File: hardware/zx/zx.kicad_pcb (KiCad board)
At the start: 2 copper layers, 71.6 x 59.9 mm, 46 parts, among them U1 CH559L, U2 CH446Q, Y1 12MHz

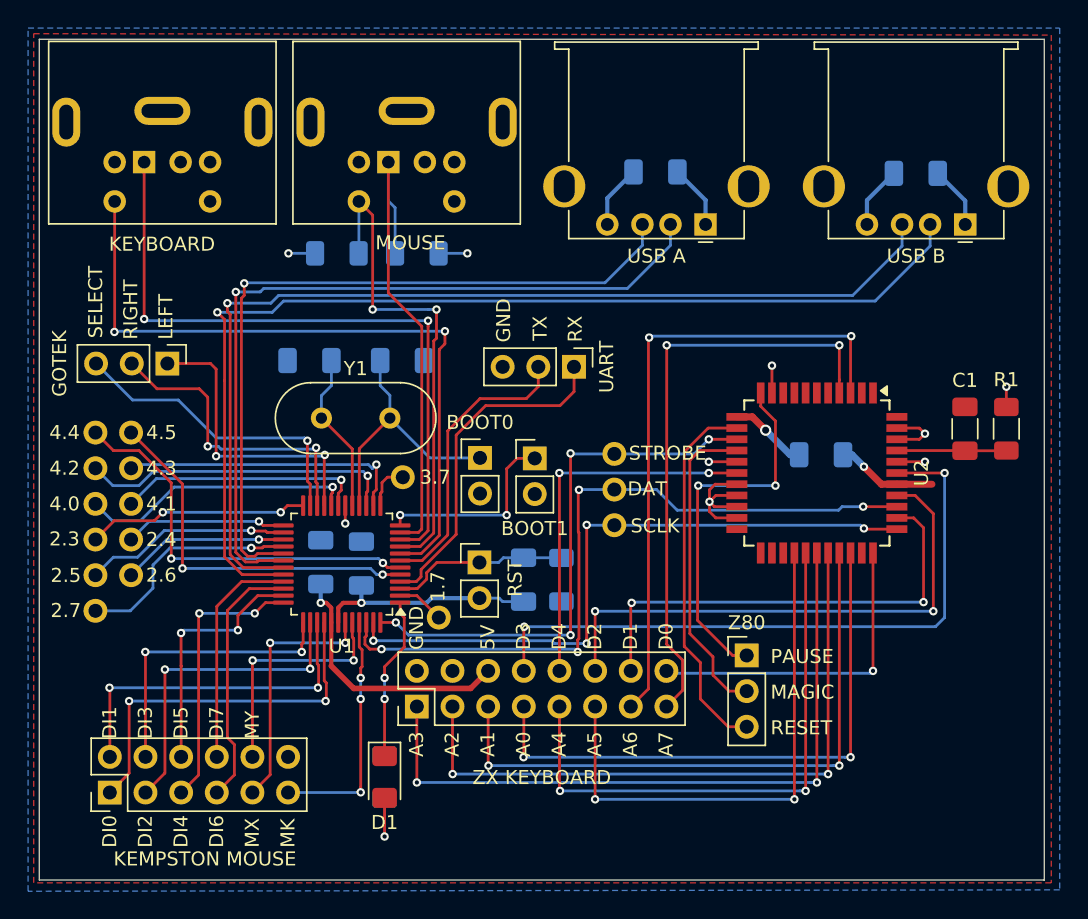
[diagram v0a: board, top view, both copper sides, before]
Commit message: PCB: replace +5V front face fill with tracks.
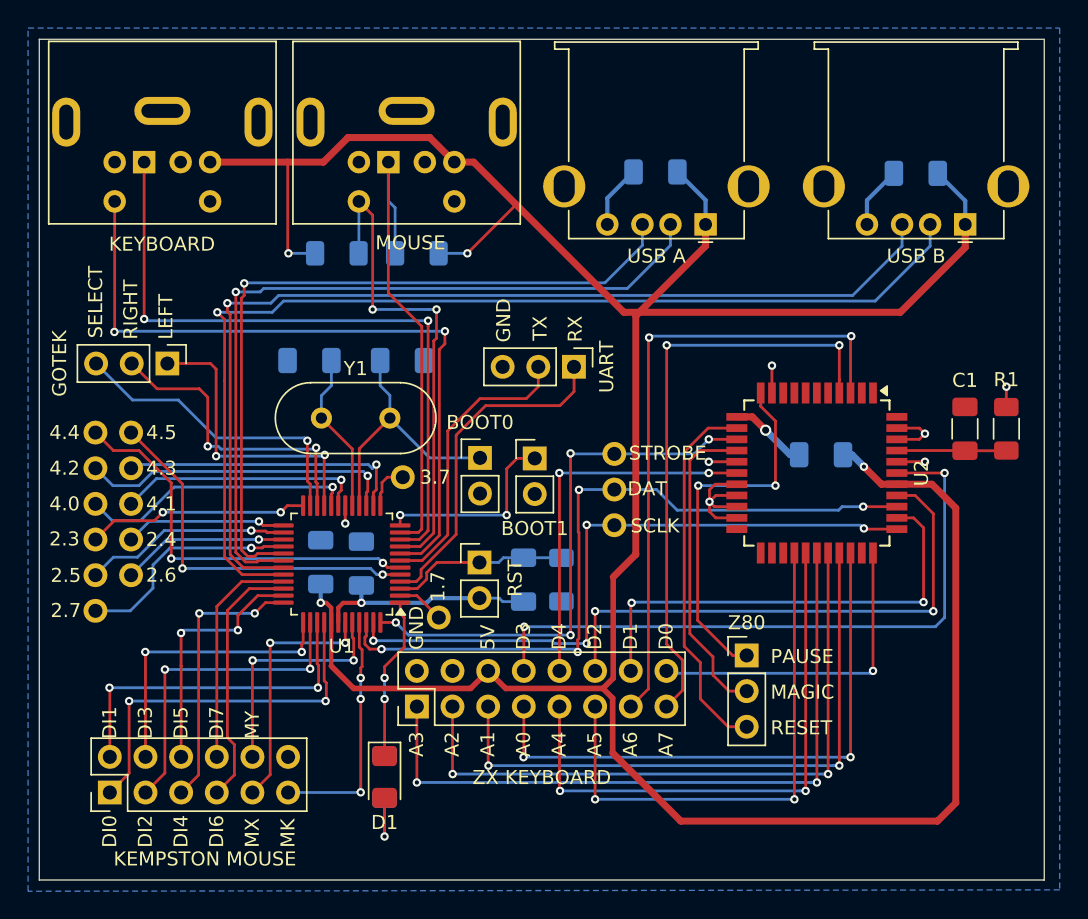
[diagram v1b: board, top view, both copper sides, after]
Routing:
- net +5V: track 38.9 -> 213.7 mm
- removed copper zone on F.Cu, net +5V
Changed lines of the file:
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@@
 	)
 	(segment
+		(start 130.95 108.75)
+		(end 129.57 108.75)
+		(width 0.5)
+		(layer "F.Cu")
+		(net 2)
+	)
+	(segment
+		(start 120.25 108.75)
+		(end 117.7 108.75)
+		(width 0.5)
+		(layer "F.Cu")
+		(net 2)
+	)
+	(segment
+		(start 140.85 150.85)
+		(end 145.7 155.7)
+		(width 0.5)
+		(layer "F.Cu")
+		(net 2)
+	)
+	(segment
 		(start 120.45 140.15)
 		(end 120.05 140.15)
@@
 	)
 	(segment
+		(start 164 155.7)
+		(end 165.3 154.4)
+		(width 0.5)
+		(layer "F.Cu")
+		(net 2)
+	)
+	(segment
+		(start 122 107)
+		(end 120.25 108.75)
+		(width 0.5)
+		(layer "F.Cu")
+		(net 2)
+	)
+	(segment
 		(start 122.4 146.25)
 		(end 120.8 144.65)
@@
 	)
 	(segment
+		(start 133.23 146.25)
+		(end 140.157767 146.25)
+		(width 0.4)
+		(layer "F.Cu")
+		(net 2)
+	)
+	(segment
+		(start 140.157767 146.25)
+		(end 140.89 145.517767)
+		(width 0.4)
+		(layer "F.Cu")
+		(net 2)
+	)
+	(segment
+		(start 140.89 145.517767)
+		(end 140.89 138.31)
+		(width 0.4)
+		(layer "F.Cu")
+		(net 2)
+	)
+	(segment
+		(start 140.157767 146.25)
+		(end 140.85 146.942233)
+		(width 0.4)
+		(layer "F.Cu")
+		(net 2)
+	)
+	(segment
+		(start 140.85 146.942233)
+		(end 140.85 150.85)
+		(width 0.4)
+		(layer "F.Cu")
+		(net 2)
+	)
+	(segment
+		(start 142.5 136.7)
+		(end 142.5 119.7)
+		(width 0.5)
+		(layer "F.Cu")
+		(net 2)
+	)
+	(segment
+		(start 161.35 119.45)
+		(end 165.97 114.83)
+		(width 0.5)
+		(layer "F.Cu")
+		(net 2)
+	)
+	(segment
+		(start 165.97 114.83)
+		(end 165.97 113.19)
+		(width 0.5)
+		(layer "F.Cu")
+		(net 2)
+	)
+	(segment
+		(start 142.75 119.45)
+		(end 161.35 119.45)
+		(width 0.5)
+		(layer "F.Cu")
+		(net 2)
+	)
+	(segment
 		(start 131.98 145)
 		(end 130.73 146.25)
@@
 	)
 	(segment
+		(start 117.7 115.2)
+		(end 117.7 108.75)
+		(width 0.2)
+		(layer "F.Cu")
+		(net 2)
+	)
+	(segment
+		(start 130.5 115.25)
+		(end 133.95 111.8)
+		(width 0.2)
+		(layer "F.Cu")
+		(net 2)
+	)
+	(segment
+		(start 145.7 155.7)
+		(end 164 155.7)
+		(width 0.5)
+		(layer "F.Cu")
+		(net 2)
+	)
+	(segment
+		(start 141.65 119.45)
+		(end 133.95 111.75)
+		(width 0.5)
+		(layer "F.Cu")
+		(net 2)
+	)
+	(segment
+		(start 140.89 138.31)
+		(end 142.5 136.7)
+		(width 0.5)
+		(layer "F.Cu")
+		(net 2)
+	)
+	(segment
+		(start 142.75 119.45)
+		(end 147.47 114.73)
+		(width 0.5)
+		(layer "F.Cu")
+		(net 2)
+	)
+	(segment
+		(start 142.75 119.45)
+		(end 141.65 119.45)
+		(width 0.5)
+		(layer "F.Cu")
+		(net 2)
+	)
+	(segment
+		(start 131.98 145)
+		(end 133.23 146.25)
+		(width 0.4)
+		(layer "F.Cu")
+		(net 2)
+	)
+	(segment
+		(start 165.3 133.4)
+		(end 163.6 131.7)
+		(width 0.5)
+		(layer "F.Cu")
+		(net 2)
+	)
+	(segment
+		(start 142.5 119.7)
+		(end 142.75 119.45)
+		(width 0.5)
+		(layer "F.Cu")
+		(net 2)
+	)
+	(segment
 		(start 130.73 146.25)
 		(end 122.4 146.25)
@@
 	)
 	(segment
+		(start 127.82 107)
+		(end 122 107)
+		(width 0.5)
+		(layer "F.Cu")
+		(net 2)
+	)
+	(segment
+		(start 117.7 108.75)
+		(end 112.17 108.75)
+		(width 0.5)
+		(layer "F.Cu")
+		(net 2)
+	)
+	(segment
 		(start 160 131.7)
 		(end 161.1 131.7)
@@
 	)
 	(segment
+		(start 133.95 111.8)
+		(end 133.95 111.75)
+		(width 0.2)
+		(layer "F.Cu")
+		(net 2)
+	)
+	(segment
 		(start 120.8 144.65)
 		(end 120.8 141.55)
@@
 	)
 	(segment
+		(start 165.3 154.4)
+		(end 165.3 133.4)
+		(width 0.5)
+		(layer "F.Cu")
+		(net 2)
+	)
+	(segment
+		(start 129.57 108.75)
+		(end 127.82 107)
+		(width 0.5)
+		(layer "F.Cu")
+		(net 2)
+	)
+	(segment
+		(start 133.95 111.75)
+		(end 130.95 108.75)
+		(width 0.5)
+		(layer "F.Cu")
+		(net 2)
+	)
+	(segment
 		(start 161.1 131.7)
 		(end 163.6 131.7)
@@
 	)
 	(segment
+		(start 147.47 114.73)
+		(end 147.47 113.19)
+		(width 0.5)
+		(layer "F.Cu")
+		(net 2)
+	)
+	(segment
 		(start 120.8 140.5)
 		(end 120.45 140.15)
@@
 		(net 2)
 	)
+	(segment
+		(start 117.75 115.25)
+		(end 117.7 115.2)
+		(width 0.2)
+		(layer "F.Cu")
+		(net 2)
+	)
 	(via
 		(at 117.75 115.25)
@@
 			)
 		)
-	)
-	(zone
-		(net 2)
-		(net_name "+5V")
-		(layer "F.Cu")
-		(hatch edge 0.5)
-		(connect_pads
-			(clearance 0.5)
-		)
-		(min_thickness 0.25)
-		(filled_areas_thickness no)
-		(fill
-			(thermal_gap 0.5)
-			(thermal_bridge_width 0.5)
-		)
-		(polygon
-			(pts
-				(xy 99.6 99.6) (xy 172.1 99.7) (xy 172.1 160.1) (xy 99.6 160.1)
-			)
-		)

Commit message: Sync PCB footprints designators with schematic. Hide PCB footprints designators text. Add footprints description text. Alter GND in track.
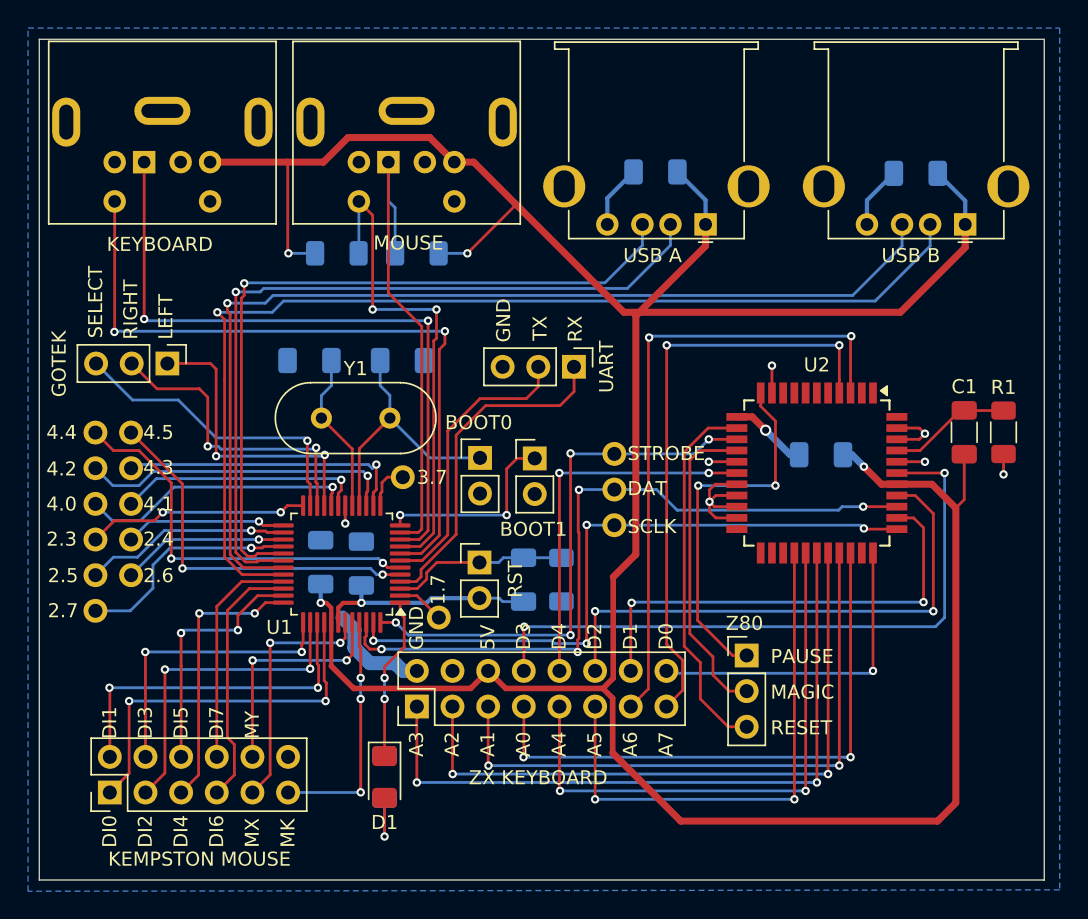
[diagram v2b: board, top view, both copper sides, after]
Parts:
- J1: renamed from ZX KEYBOARD
- J4: renamed from USB A
- J5: renamed from USB B
- J8: renamed from KEMPSTON MOUSE
- moved R1 0.32 mm to (168.7, 128.0), turned to 90 degrees
- moved C1 0.25 mm to (165.9, 128.0), turned to 90 degrees
- renumbered 1.7 to J10, 4.5 to J11, 4.4 to J12, 3.7 to J13, 4.3 to J14, 4.2 to J15, 4.1 to J16, 4.0 to J17, 2.3 to J18, 2.4 to J19, GOTEK to J2, 2.5 to J20, 2.6 to J21, 2.7 to J22, DAT to J23, SCLK to J24, STROBE to J25, UART to J3, KEYBOARD to J6, MOUSE to J7, Z80 to J9, RST to SW1, BOOT0 to SW2, BOOT1 to SW3
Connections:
- J8 pad 12: unconnected-(J8-Pin_12-Pad12) -> GND
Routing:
- net GND: track 37.5 -> 45.2 mm
- net +5V: track 213.7 -> 217.8 mm
- net Net-(U2-RST): track 7.81 -> 8.79 mm
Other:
- board text added: "1.7"
- board text added: "2.3"
- board text added: "2.4"
- board text added: "2.5"
- board text added: "2.6"
- board text added: "2.7"
- board text added: "3.7"
- board text added: "4.0"
- board text added: "4.1"
- board text added: "4.2"
- board text added: "4.3"
- board text added: "4.4"
- board text added: "4.5"
- board text added: "BOOT0"
- board text added: "BOOT1"
- board text added: "DAT"
- board text added: "GOTEK"
- board text added: "KEMPSTON MOUSE"
- board text added: "KEYBOARD"
- board text added: "MOUSE"
- board text added: "RST"
- board text added: "SCLK"
- board text added: "STROBE"
- board text added: "UART"
- board text added: "USB A"
- board text added: "USB B"
- board text added: "Z80"
- board text added: "ZX KEYBOARD"

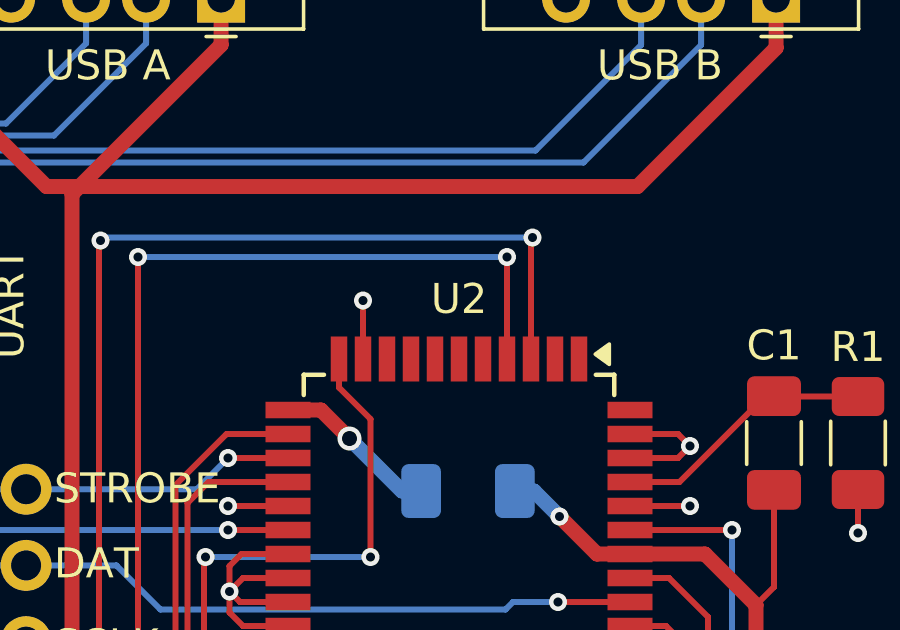
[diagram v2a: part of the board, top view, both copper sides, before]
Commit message: CH446Q output Z80 control signals PAUSE, MAGIC, RESET have common input connected to GND.
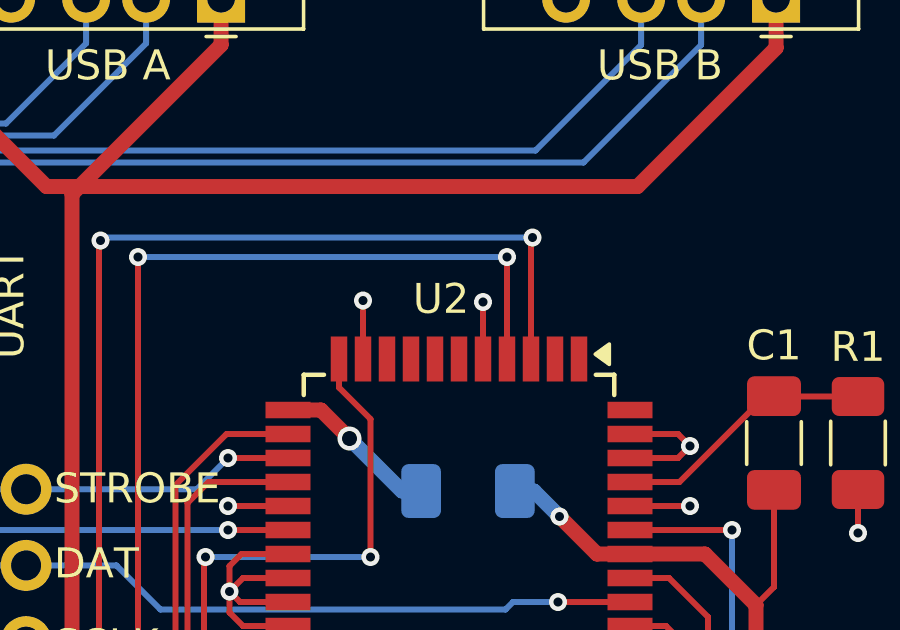
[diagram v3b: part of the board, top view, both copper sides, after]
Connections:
- U2 pad 5: unconnected-(U2-X8-Pad5) -> GND
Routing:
- net GND: track 45.2 -> 47.1 mm, vias 8 -> 9
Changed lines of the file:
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@@
 	(net 74 "unconnected-(U2-NC-Pad9)")
 	(net 75 "unconnected-(U2-X15-Pad2)")
-	(net 76 "unconnected-(U2-X8-Pad5)")
-	(net 77 "unconnected-(U2-X12-Pad25)")
-	(net 78 "unconnected-(U2-NC-Pad32)")
-	(net 79 "unconnected-(U2-X11-Pad8)")
-	(net 80 "unconnected-(U2-X9-Pad6)")
-	(net 81 "unconnected-(U2-NC-Pad44)")
-	(net 82 "unconnected-(U2-X13-Pad24)")
-	(net 83 "unconnected-(U2-NC-Pad23)")
-	(net 84 "unconnected-(U2-NC-Pad22)")
+	(net 76 "unconnected-(U2-X12-Pad25)")
+	(net 77 "unconnected-(U2-NC-Pad32)")
+	(net 78 "unconnected-(U2-X11-Pad8)")
+	(net 79 "unconnected-(U2-X9-Pad6)")
+	(net 80 "unconnected-(U2-NC-Pad44)")
+	(net 81 "unconnected-(U2-X13-Pad24)")
+	(net 82 "unconnected-(U2-NC-Pad23)")
+	(net 83 "unconnected-(U2-NC-Pad22)")
 	(footprint "THT_Pin:THT_Pin_Vertical"
 		(layer "F.Cu")
@@
 		(tags "QFP 0.8")
 		(property "Reference" "U2"
-			(at -7.7 0 180)
+			(at -7.7 0.6 180)
 			(layer "F.SilkS")
 			(effects
@@
 			(size 1.5 0.55)
 			(layers "F.Cu" "F.Paste" "F.Mask")
-			(net 76 "unconnected-(U2-X8-Pad5)")
+			(net 3 "GND")
 			(pinfunction "X8")
-			(pintype "input+no_connect")
+			(pintype "input")
 		)
 		(pad "6" smd rect
@@
 			(size 1.5 0.55)
 			(layers "F.Cu" "F.Paste" "F.Mask")
-			(net 80 "unconnected-(U2-X9-Pad6)")
+			(net 79 "unconnected-(U2-X9-Pad6)")
 			(pinfunction "X9")
 			(pintype "input+no_connect")
@@
 			(size 1.5 0.55)
 			(layers "F.Cu" "F.Paste" "F.Mask")
-			(net 79 "unconnected-(U2-X11-Pad8)")
+			(net 78 "unconnected-(U2-X11-Pad8)")
 			(pinfunction "X11")
 			(pintype "input+no_connect")
@@
 			(size 1.5 0.55)
 			(layers "F.Cu" "F.Paste" "F.Mask")
-			(net 84 "unconnected-(U2-NC-Pad22)")
+			(net 83 "unconnected-(U2-NC-Pad22)")
 			(pinfunction "NC")
 			(pintype "passive+no_connect")
@@
 			(size 1.5 0.55)
 			(layers "F.Cu" "F.Paste" "F.Mask")
-			(net 83 "unconnected-(U2-NC-Pad23)")
+			(net 82 "unconnected-(U2-NC-Pad23)")
 			(pinfunction "NC")
 			(pintype "passive+no_connect")
@@
 			(size 1.5 0.55)
 			(layers "F.Cu" "F.Paste" "F.Mask")
-			(net 82 "unconnected-(U2-X13-Pad24)")
+			(net 81 "unconnected-(U2-X13-Pad24)")
 			(pinfunction "X13")
 			(pintype "input+no_connect")
@@
 			(size 1.5 0.55)
 			(layers "F.Cu" "F.Paste" "F.Mask")
-			(net 77 "unconnected-(U2-X12-Pad25)")
+			(net 76 "unconnected-(U2-X12-Pad25)")
 			(pinfunction "X12")
 			(pintype "input+no_connect")
@@
 			(size 1.5 0.55)
 			(layers "F.Cu" "F.Paste" "F.Mask")
-			(net 78 "unconnected-(U2-NC-Pad32)")
+			(net 77 "unconnected-(U2-NC-Pad32)")
 			(pinfunction "NC")
 			(pintype "passive+no_connect")
@@
 			(size 1.5 0.55)
 			(layers "F.Cu" "F.Paste" "F.Mask")
-			(net 81 "unconnected-(U2-NC-Pad44)")
+			(net 80 "unconnected-(U2-NC-Pad44)")
 			(pinfunction "NC")
 			(pintype "passive+no_connect")
@@
 	)
 	(segment
+		(start 156.2 125.2)
+		(end 156.2 123.3)
+		(width 0.2)
+		(layer "F.Cu")
+		(net 3)
+	)
+	(segment
 		(start 161.1 128.5)
 		(end 162.7 128.5)
@@
 		(size 0.6)
 		(drill 0.3)
+		(layers "F.Cu" "B.Cu")
+		(net 3)
+	)
+	(via
+		(at 156.2 123.3)
+		(size 0.6)
+		(drill 0.3)

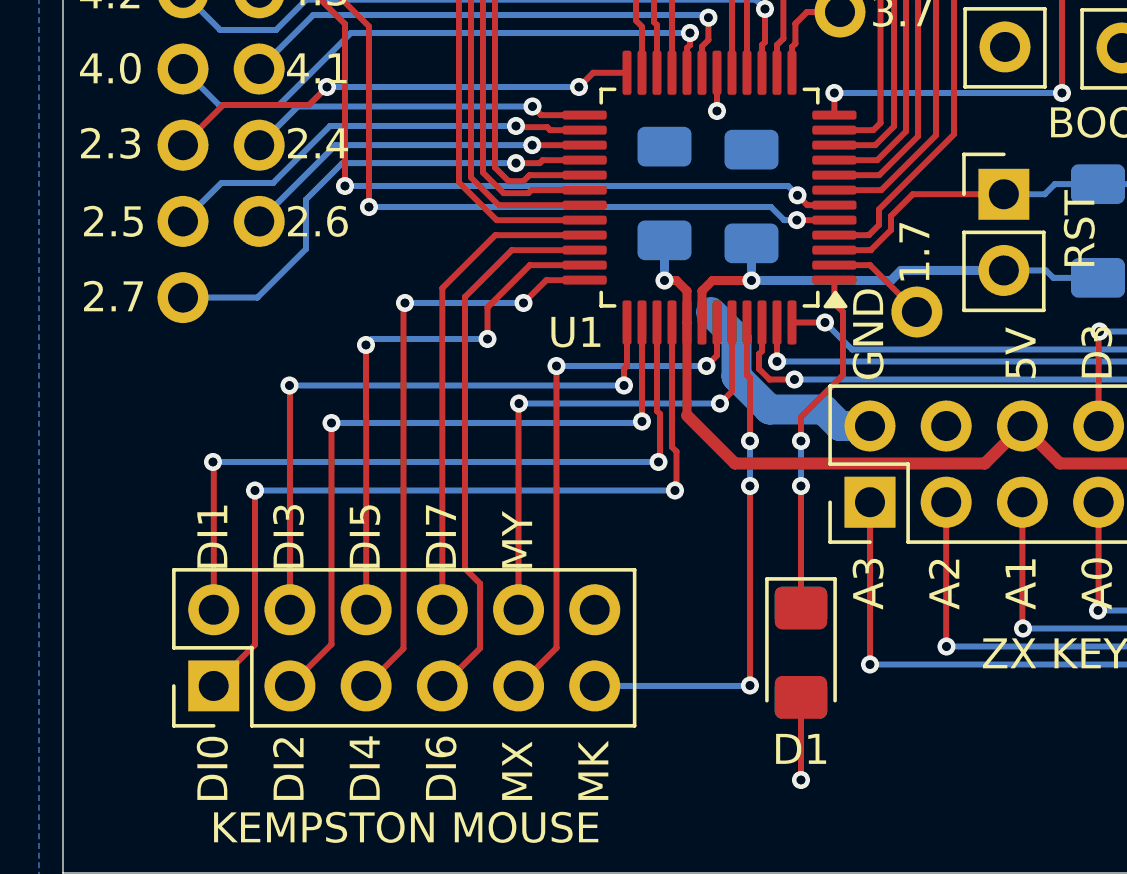
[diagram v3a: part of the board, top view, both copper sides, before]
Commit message: Reserve P1.6 for Kempston Joystick DI write strobe (JOY). Move activity LED to P1.7. Add free-standing GND pin. Add J8 GND label.
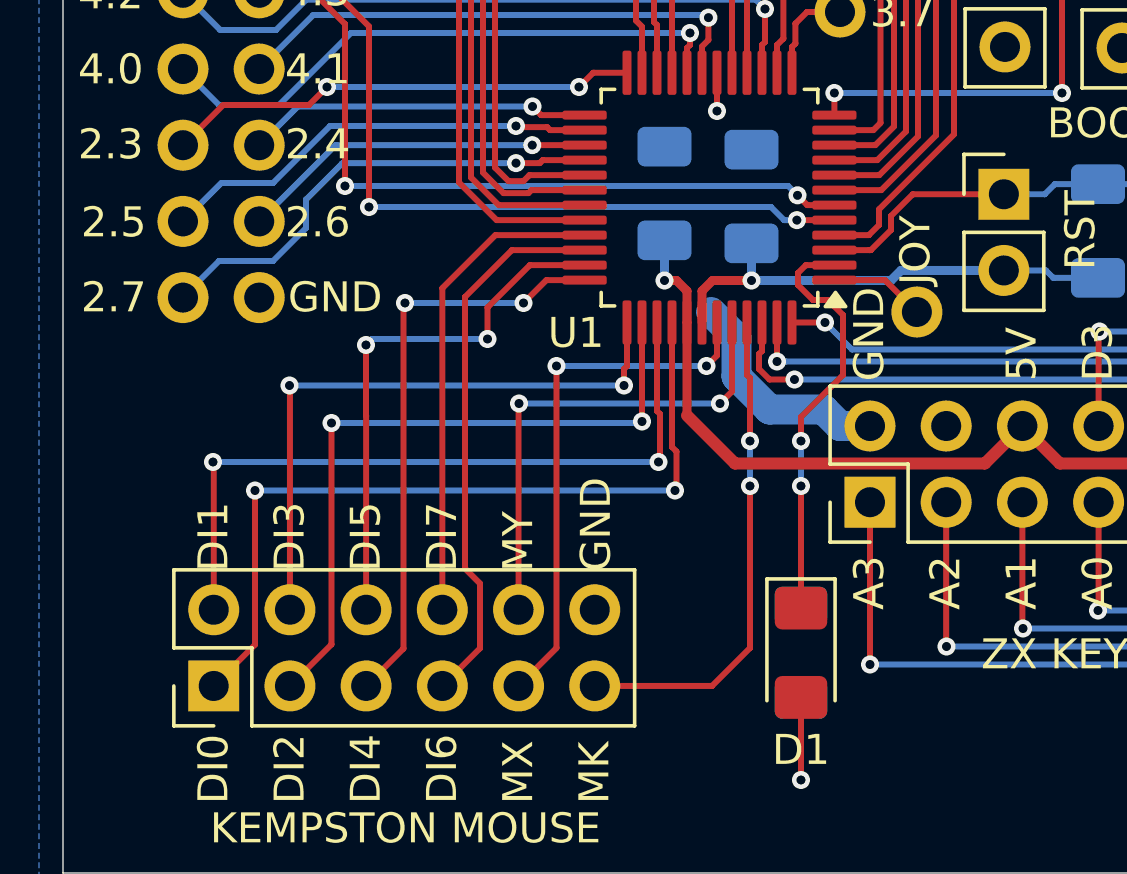
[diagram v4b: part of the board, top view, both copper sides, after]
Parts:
- added J26: Conn_01x01, THT_Pin:THT_Pin_Vertical, F.Cu at (106.5, 140.7)
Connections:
- D1 pad 1: /P1_6 -> /P1_7
- J10 pad 1: /P1_7 -> /JOY
- U1 pad 1: /P1_6 -> /JOY
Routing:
- net /P1_6: track 11.6 -> 0.00 mm, vias 2 -> 0
- net /P1_7: track 3.40 -> 14.0 mm, vias 0 -> 2
- net /JOY: track 0.00 -> 3.19 mm
- net /MKEY: track 17.3 -> 16.6 mm, vias 3 -> 2
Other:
- board text added: "JOY"
- board text removed: "1.7"
